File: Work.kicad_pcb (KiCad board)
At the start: 2 copper layers, 72.4 x 42.4 mm, 1 part, among them J3 ZX62R-B-5P_30_

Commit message: SCH & PCB Data
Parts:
- added A1: NJM2845DL1-33, Package_TO_SOT_SMD:TO-252-2, F.Cu at (110.4, 140.2)
- added A2: NJM12888F18, HLDC-E2:SOT-23-5, F.Cu at (108.5, 132.9)
- added A3: FT231XS-R, HLDC_E1:SOP64P599X175-20N, F.Cu at (94.2, 131.5)
- added A4: AMG8833, HLDC_E1:XDCR_AMG8833, F.Cu at (100.3, 118.2)
- added A5: MLX90640ESF-BAA-000-TU, HLDC_E1:TO292P930H600-4, F.Cu at (87.6, 117.4)
- added C1: 0.01u, HLDC_E1:C_0603_1608Metric, F.Cu at (125.8, 135.3)
- added C10: 0.1u, HLDC_E1:C_0603_1608Metric, F.Cu at (116.7, 118.3)
- added C11: 0.01u, HLDC_E1:C_0603_1608Metric, F.Cu at (109.2, 125.1)
- added C12: 0.47u, HLDC_E1:C_0603_1608Metric, F.Cu at (108.9, 147.5)
- added C13: 1u, HLDC_E1:C_0603_1608Metric, F.Cu at (116.5, 144.5)
- added C14: 1u, HLDC_E1:C_0603_1608Metric, F.Cu at (114.8, 144.5)
- added C15: 0.1u, HLDC_E1:C_0603_1608Metric, F.Cu at (105.7, 133.2)
- added C16: 0.01u, HLDC_E1:C_0603_1608Metric, F.Cu at (111.7, 131.0)
- added C17: 0.47u, HLDC_E1:C_0603_1608Metric, F.Cu at (109.0, 129.3)
- added C18: 0.01u, HLDC_E1:C_0603_1608Metric, F.Cu at (107.5, 129.3)
- added C19: 10u, HLDC_E1:F920J106MPA, F.Cu at (103.7, 141.5)
- added C2: 0.01u, HLDC_E1:C_0603_1608Metric, F.Cu at (124.9, 124.4)
- added C20: 0.1u, HLDC_E1:C_0603_1608Metric, F.Cu at (105.8, 142.5)
- added C21: 0.1u, HLDC_E1:C_0603_1608Metric, F.Cu at (95.7, 136.1)
- added C22: 0.1u, HLDC_E1:C_0603_1608Metric, F.Cu at (95.7, 137.6)
- added C23: 22p, HLDC_E1:C_0603_1608Metric, F.Cu at (88.9, 139.1)
- added C24: 22p, HLDC_E1:C_0603_1608Metric, F.Cu at (95.0, 139.1)
- added C25: 0.1u, HLDC_E1:C_0603_1608Metric, F.Cu at (96.6, 126.9)
- added C26: 10u, HLDC_E1:C_0603_1608Metric, B.Cu at (96.9, 114.2)
- added C27: 1u, HLDC_E1:C_0603_1608Metric, B.Cu at (103.4, 116.9)
- added C28: 1.5u, HLDC_E1:C_0603_1608Metric, B.Cu at (97.3, 116.9)
- added C29: 1u, HLDC_E1:C_0603_1608Metric, B.Cu at (88.2, 117.0)
- added C3: 0.1u, HLDC_E1:C_0603_1608Metric, F.Cu at (124.2, 135.3)
- added C30: 0.1u, HLDC_E1:C_0603_1608Metric, B.Cu at (88.2, 118.5)
- added C4: 1u, HLDC_E1:C_0603_1608Metric, F.Cu at (126.5, 114.0)
- added C5: 0.1u, HLDC_E1:C_0603_1608Metric, F.Cu at (124.9, 114.0)
- added C6: 0.1u, HLDC_E1:C_0603_1608Metric, F.Cu at (86.2, 124.1)
- added C7: 0.1u, HLDC_E1:C_0603_1608Metric, F.Cu at (84.6, 124.1)
- added C8: 0.1u, HLDC_E1:C_0603_1608Metric, F.Cu at (126.1, 143.9)
- added C9: 1000, HLDC_E1:C_0603_1608Metric, F.Cu at (126.1, 142.2)
- added D1: OSHR1608C1A, HLDC_E1:D_0603, F.Cu at (135.6, 136.6)
- added D3: OSHR1608C1A, HLDC_E1:D_0603, F.Cu at (120.0, 146.7)
- added J1: CON_5P, HLDC-E2:CONN_S5B-ZR_JST, F.Cu at (141.0, 144.0)
- added J2: CON_5P, HLDC-E2:CONN_S5B-ZR_JST, F.Cu at (130.5, 144.0)
- added Q1: DTC114EKA, Package_TO_SOT_SMD:SC-59, F.Cu at (101.4, 129.6)
- added Q2: DTC114EKA, Package_TO_SOT_SMD:SC-59, F.Cu at (101.4, 133.6)
- added R1: 10k, HLDC_E1:R_0603_1608Metric, F.Cu at (122.5, 135.3)
- added R10: 10k, HLDC_E1:R_0603_1608Metric, F.Cu at (116.7, 121.4)
- added R11: 10k, HLDC_E1:R_0603_1608Metric, F.Cu at (112.3, 125.1)
- added R12: 27, HLDC_E1:R_0603_1608Metric, F.Cu at (92.7, 138.3)
- added R13: 27, HLDC_E1:R_0603_1608Metric, F.Cu at (91.2, 138.3)
- added R14: 470, HLDC_E1:R_0603_1608Metric, F.Cu at (120.0, 145.2)
- added R15: 10k, HLDC_E1:R_0603_1608Metric, F.Cu at (135.6, 138.2)
- added R16: 470, HLDC_E1:R_0603_1608Metric, F.Cu at (139.4, 139.2)
- added R17: 20, HLDC_E1:R_0603_1608Metric, B.Cu at (103.4, 118.4)
- added R18: 10k, HLDC_E1:R_0603_1608Metric, B.Cu at (99.4, 120.6)
- added R2: 10k, HLDC_E1:R_0603_1608Metric, F.Cu at (124.8, 122.8)
- added R3: 10k, HLDC_E1:R_0603_1608Metric, F.Cu at (100.6, 108.7)
- added R4: 10k, HLDC_E1:R_0603_1608Metric, F.Cu at (103.7, 108.7)
- added R5: 10k, HLDC_E1:R_0603_1608Metric, F.Cu at (124.9, 117.7)
- added R6: 10k, HLDC_E1:R_0603_1608Metric, F.Cu at (141.0, 139.2)
- added R7: 10k, HLDC_E1:R_0603_1608Metric, F.Cu at (142.5, 139.2)
- added R8: 10k, HLDC_E1:R_0603_1608Metric, F.Cu at (144.0, 139.2)
- added R9: 10k, HLDC_E1:R_0603_1608Metric, F.Cu at (145.5, 139.2)
- added S1: TVAF06-A020B-R, HLDC_E1:TVAF06A020BR, F.Cu at (123.5, 131.5)
- added S2: TVAF06-A020B-R, HLDC_E1:TVAF06A020BR, F.Cu at (123.5, 127.8)
- added S3: TVAF06-A020B-R, HLDC_E1:TVAF06A020BR, F.Cu at (113.5, 119.8)
- added S4: A6H-4102-P, HLDC-E2:SW_DIP_SPSTx04_Slide_Omron_A6H-4101_W6.15mm_P1.27mm, F.Cu at (115.3, 111.9)
- added S5: TVAF06-A020B-R, HLDC_E1:TVAF06A020BR, F.Cu at (109.9, 119.8)
- added S6: TVAF06-A020B-R, HLDC_E1:TVAF06A020BR, F.Cu at (130.7, 138.2)
- added TP5: TP_FL, HLDC_E1:HLDC_logo2, F.Cu at (152.1, 124.9)
- added U1: ESP32-WROOM-32E, HLDC_E1:ESP32WROOM32E-Hole, F.Cu at (129.5, 133.0)
- added U2: XM125, HLDC-E2:XM125_ACC, F.Cu at (97.2, 117.9)
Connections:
- J3 pad 1: unconnected-(J3-VCC-Pad1) -> VBUS
- J3 pad 2: unconnected-(J3-D--Pad2) -> Net-(J3-D-)
- J3 pad 3: unconnected-(J3-D+-Pad3) -> Net-(J3-D+)
- J3 pad 5: unconnected-(J3-GND-Pad5) -> GND
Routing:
- net +3.3V: track 0.00 -> 229.4 mm, vias 0 -> 12
- net I2C_SDA: track 0.00 -> 97.3 mm, vias 0 -> 4
- net ESP_UART0_TxD: track 0.00 -> 88.3 mm, vias 0 -> 4
- net I2C_SCL: track 0.00 -> 84.7 mm, vias 0 -> 4
- net ESP_UART0_RxD: track 0.00 -> 82.0 mm, vias 0 -> 4
- net XM_UART_RxD: track 0.00 -> 78.9 mm, vias 0 -> 6
- net XM_UART_TxD: track 0.00 -> 76.3 mm, vias 0 -> 6
- net BOOT: track 0.00 -> 67.1 mm, vias 0 -> 6
- net LPM_INT: track 0.00 -> 58.9 mm, vias 0 -> 2
- net AMG_INT: track 0.00 -> 50.3 mm, vias 0 -> 4
- net EN: track 0.00 -> 49.1 mm, vias 0 -> 6
- net VBUS: track 0.00 -> 48.8 mm, vias 0 -> 5
- net ESP_UART2_RxD: track 0.00 -> 46.6 mm, vias 0 -> 2
- net ESP_UART2_TxD: track 0.00 -> 45.6 mm, vias 0 -> 2
- net DT+_4: track 0.00 -> 42.1 mm, vias 0 -> 1
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- added copper zone on B.Cu, net GND
- added copper zone on F.Cu, net GND
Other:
- outline, holes or cut-outs redrawn
- board text added: "BOOT"
- board text added: "DEBUG"
- board text added: "DT+"
- board text added: "EN"
- board text added: "ESP"
- board text added: "NRST"
- board text added: "PZ-H036Z-R0"
- board text added: "Rx"
- board text added: "Rx2"
- board text added: "SCL"
- board text added: "SDA"
- board text added: "Tx"
- board text added: "Tx2"
- board text added: "UART"
- board text added: "UART1"
- board text added: "UART2"
- board text added: "VDD"
- board text added: "XM"
- board text added: "XM-UART"
- board text added: "XMBOOT"

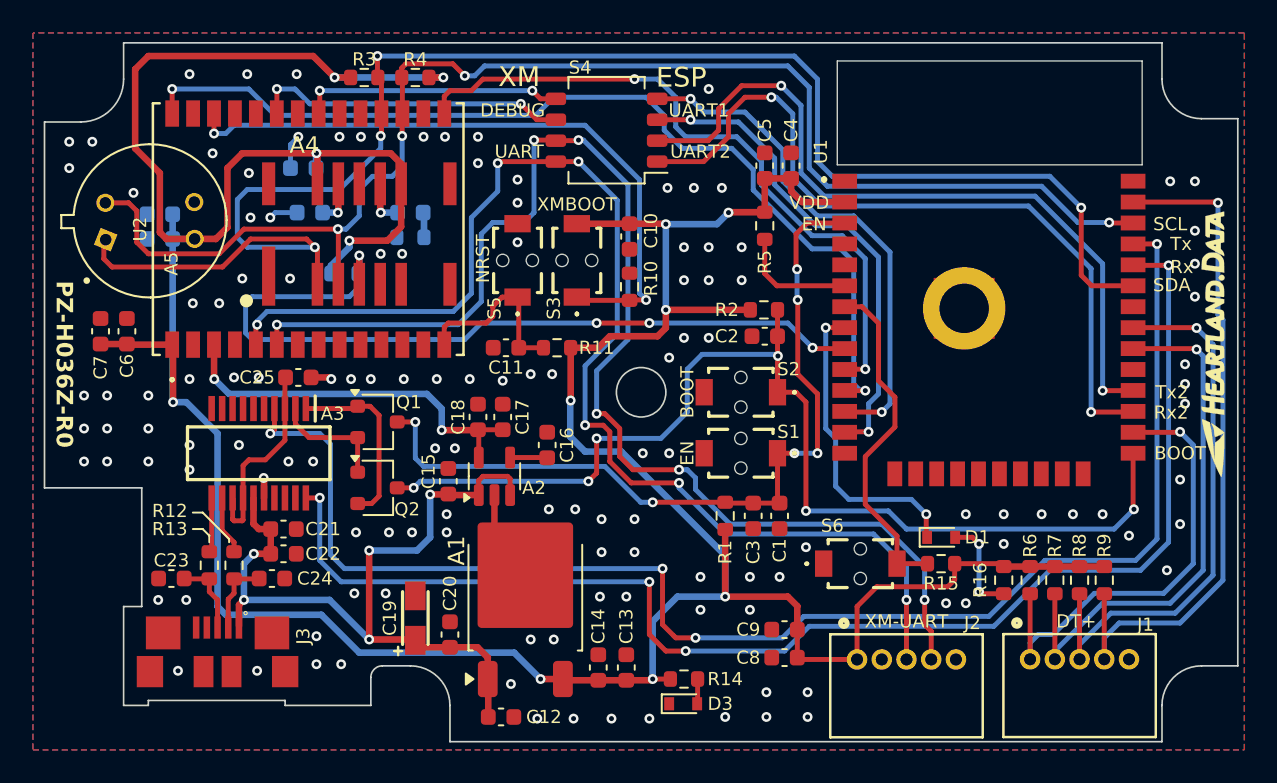
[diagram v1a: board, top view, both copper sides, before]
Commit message: DIP SW Pad Change
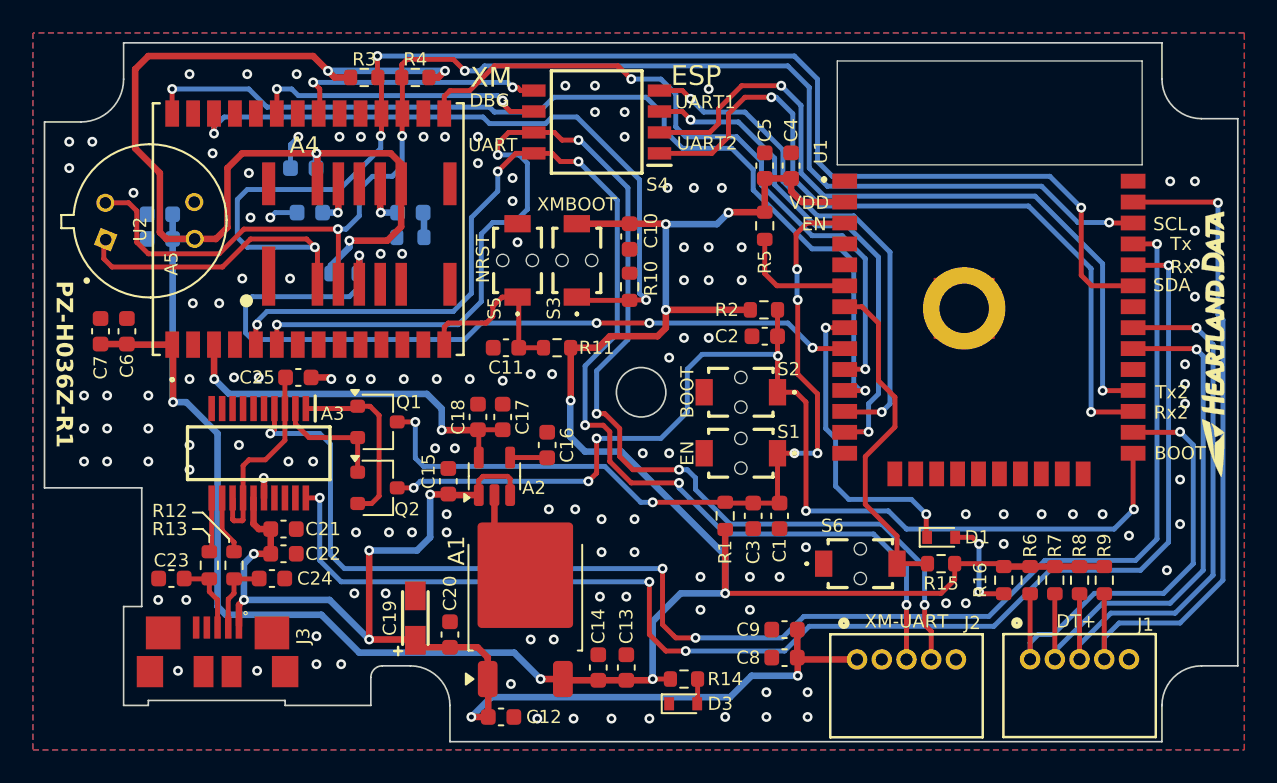
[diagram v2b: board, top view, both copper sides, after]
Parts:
- added G***: LOGO, HLDC_E1:bugless_uuum, B.Cu at (144.2, 122.9)
- added G***: LOGO, HLDC_E1:bugless_mu, B.Cu at (92.6, 138.2)
- S4: footprint HLDC-E2:SW_DIP_SPSTx04_Slide_Omron_A6H-4101_W6.15mm_P1.27mm -> HLDC_E1:SOIC127P812X230-8N
- moved S4 0.78 mm to (114.7, 111.4)
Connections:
- C8 pad 2: +3.3V -> VBUS
- C9 pad 2: +3.3V -> VBUS
- J2 pad 1: +3.3V -> VBUS
- U2 pad 24: Net-(U2-MISC_GPIO0) -> unconnected-(U2-MISC_GPIO0-Pad24)
- U2 pad 25: Net-(U2-MISC_GPIO1) -> unconnected-(U2-MISC_GPIO1-Pad25)
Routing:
- net VBUS: track 48.8 -> 77.2 mm, vias 5 -> 7
- net +3.3V: track 229.4 -> 222.9 mm
- net XM_UART_RxD: track 78.9 -> 82.2 mm
- net XM_Debug_TxD: track 19.2 -> 17.8 mm
- net XM_BOOT: track 40.4 -> 41.3 mm
- net LPM_CTL: track 41.5 -> 42.3 mm
- net ESP_UART2_TxD: track 45.6 -> 45.0 mm
- net GND: vias 131 -> 136
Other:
- board text added: "DBG"
- board text added: "PZ-H036Z-R1"
- board text removed: "DEBUG"
- board text removed: "PZ-H036Z-R0"
